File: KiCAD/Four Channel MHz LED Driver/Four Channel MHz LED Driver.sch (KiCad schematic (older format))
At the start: 81 parts, among them J1 Barrel_Jack_Switch, J10 Conn_01x08_Female, J2 Conn_01x02_Female, J3 8P8C_Shielded_x4, J4 Conn_01x05_Female, J5 Conn_01x24_Female, J6 Conn_01x03_Male, J7 Conn_01x24_Female, J8 Conn_01x03_Female, J9 Conn_01x03_Female, M1 Fan_4pin, Q2 SUM70060E, SW1 SW_SPDT, SW2 Pushbutton_with_LED_-_ELUMOAT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, SW3 Pushbutton_with_LED_-_ELUMOAT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, SW4 Pushbutton_with_LED_-_ELUMOAT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, SW5 Pushbutton_with_LED_-_ELUMOAT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, U1 12V boost, U10 LT6200CS8-10, U14 Teensy3.6, U16 SN74LV4T125PWR, U2 ASSR-1218, U3 DPBW06F-05, U4 BDJ0GA5WEFJ-E2, U5 ADP7182AUJZ-1.8-R7, U6 TMUX1204DGSR, U7 ASSR-1218, U8 ASSR-1218, U9 ASSR-1218

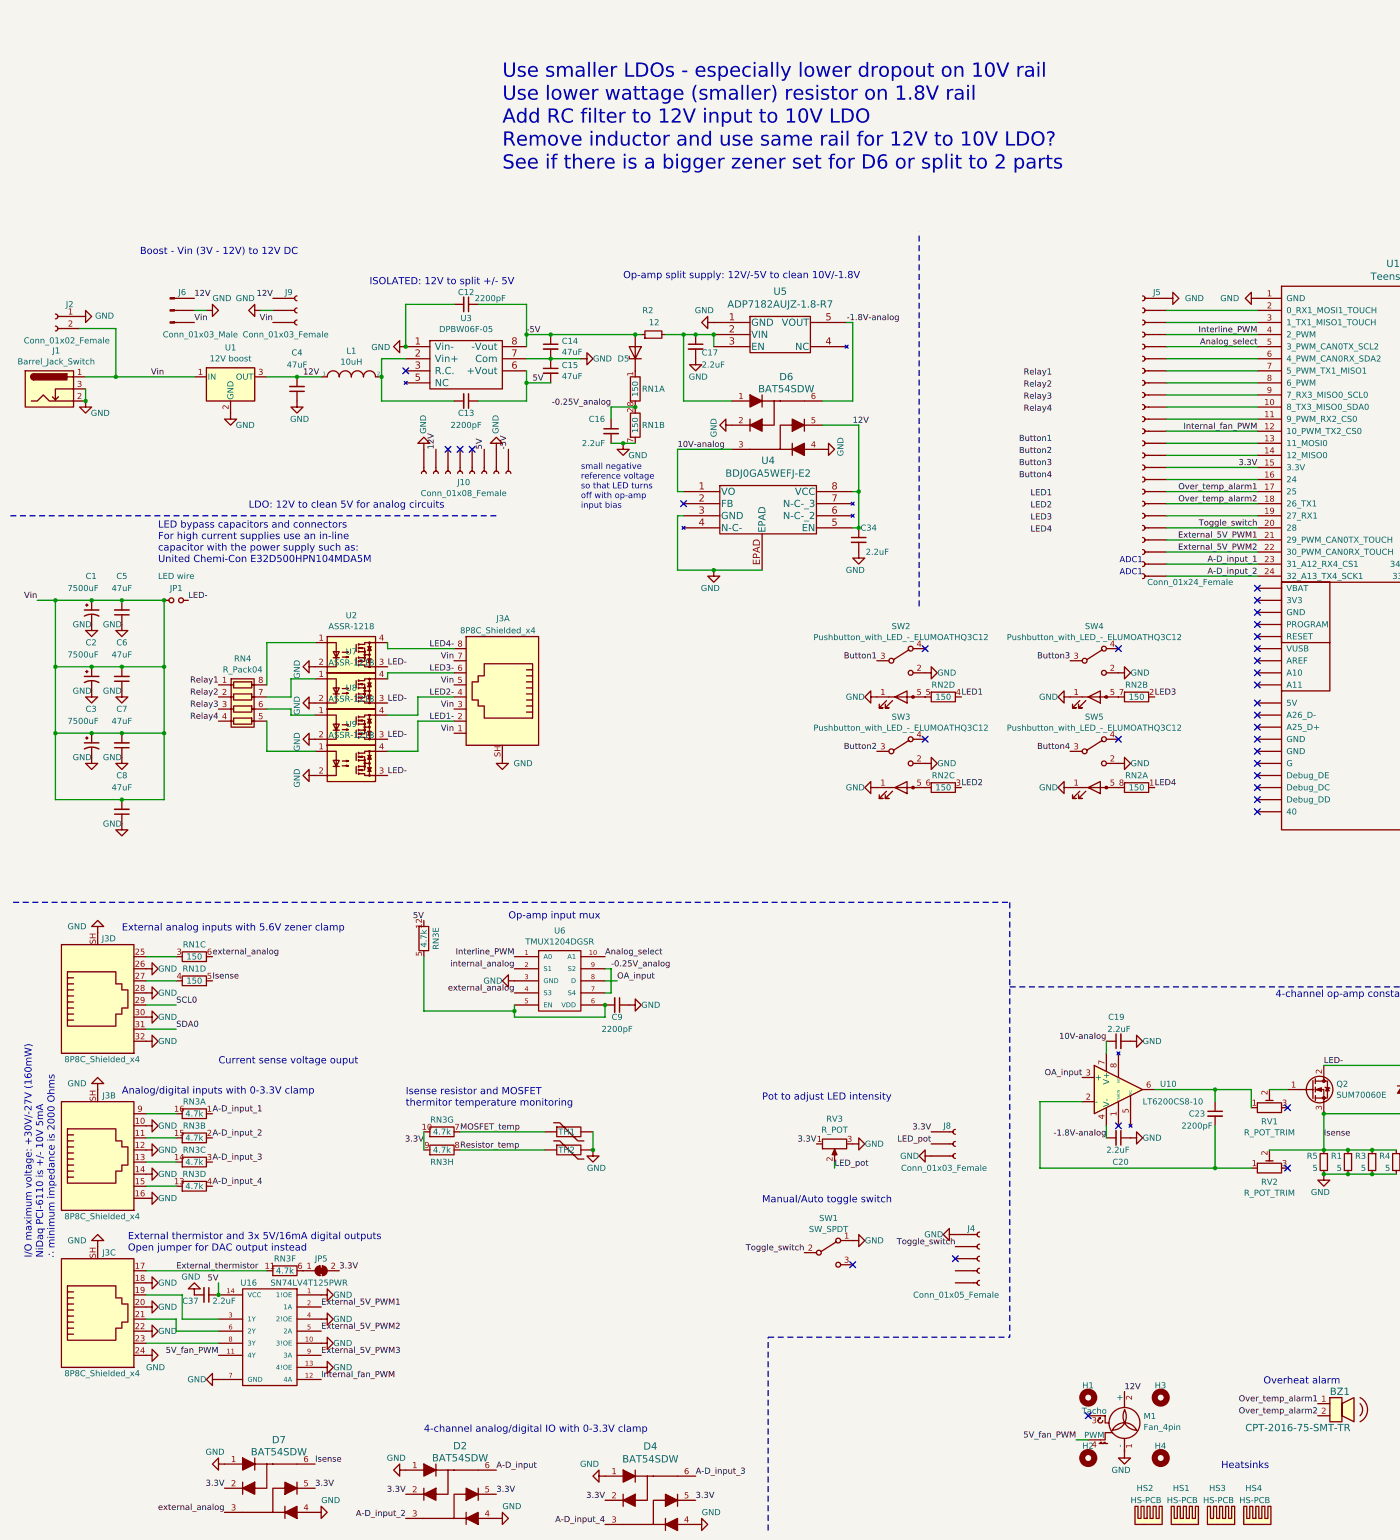
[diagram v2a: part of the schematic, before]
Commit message: Relays connected
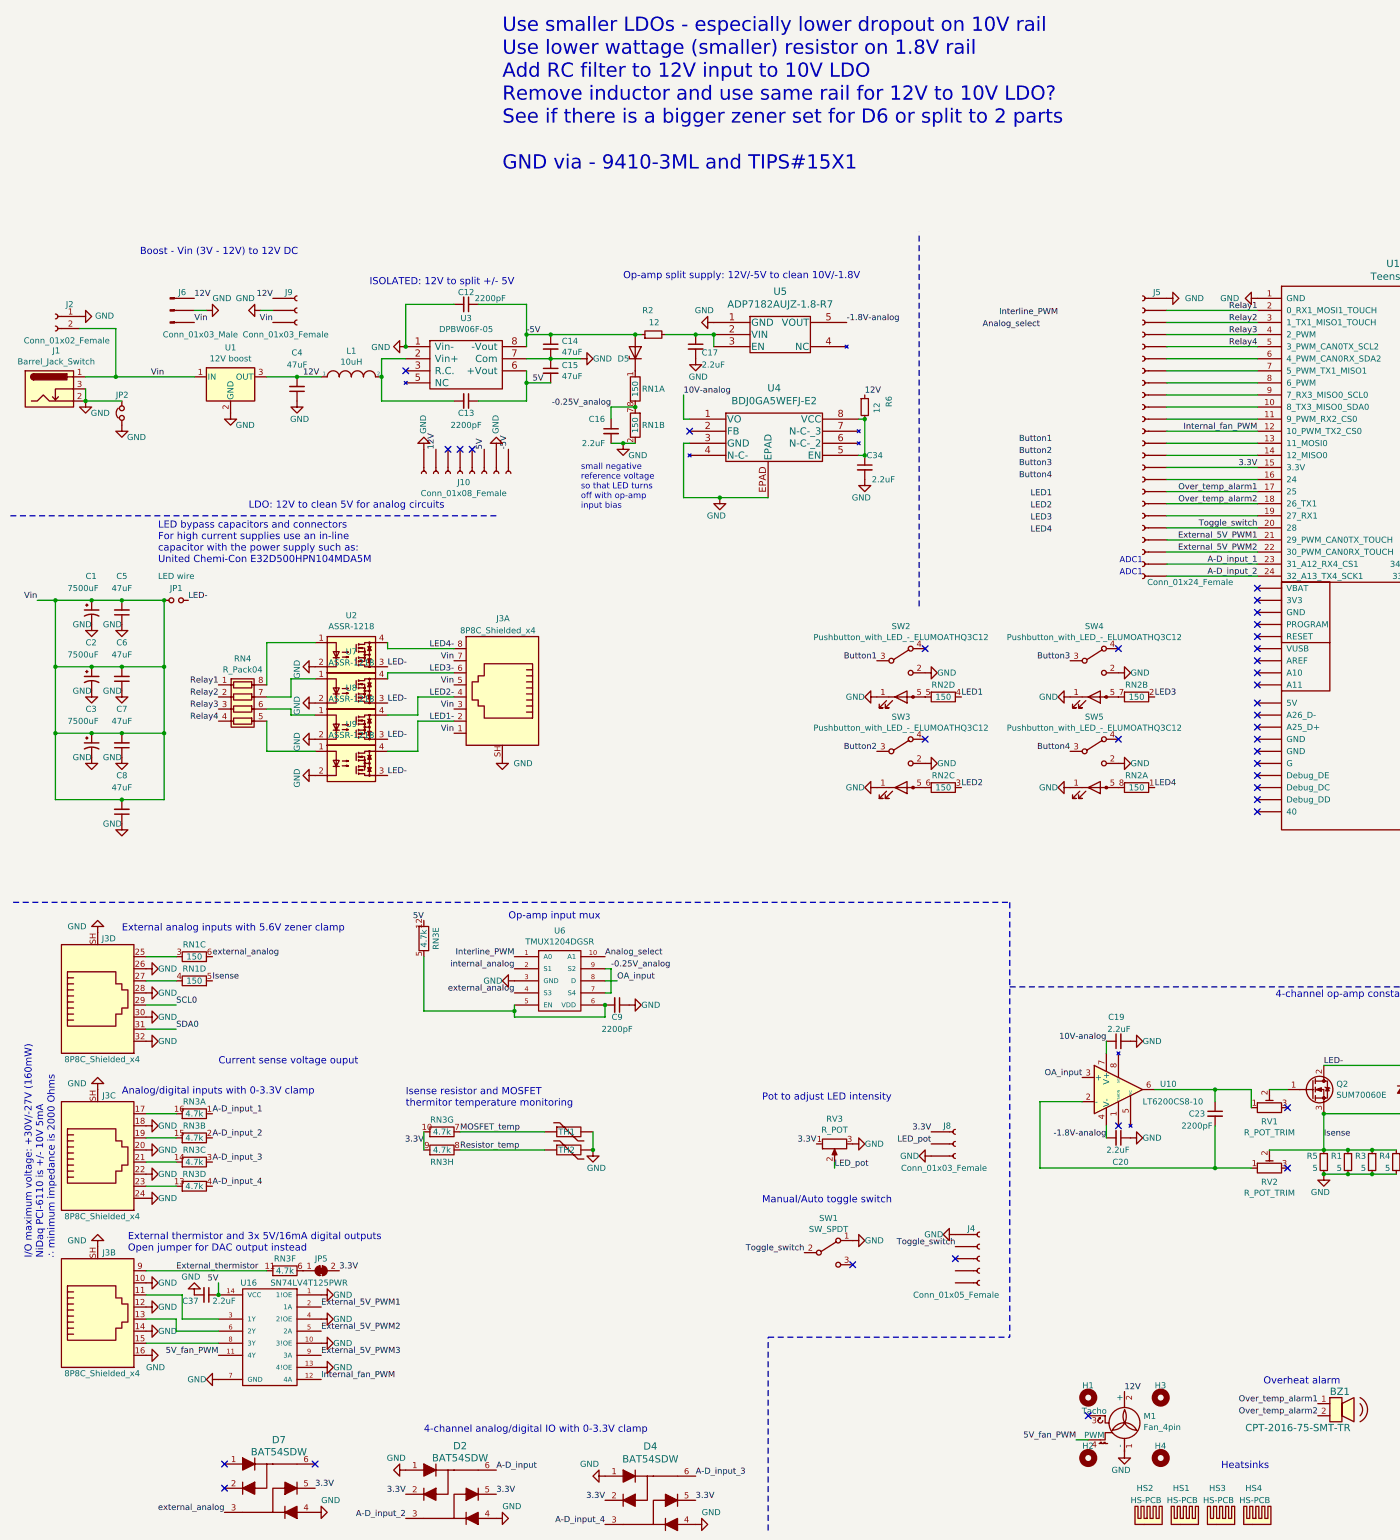
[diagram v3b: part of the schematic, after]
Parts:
- removed D6: BAT54SDW, Package_TO_SOT_SMD:SOT-363_SC-70-6, symbol Custom_parts:BAT54SDW
- added JP2: Jumper_NC_Small, Resistor_SMD:R_1206_3216Metric, symbol Device:Jumper_NC_Small
- added R6: 12, Resistor_SMD:R_1210_3225Metric, symbol Device:R_Small
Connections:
- net -0.25V_analog: now also RN1.7 (R2.2); no longer RN1.2 (R2.1)
- net 12V: now also R6.1; no longer C34.1, U4.5 (EN), U4.8 (VCC)
- net 3.3V: no longer D7.2
- net Analog_select: no longer J5.~, U14.5 (3_PWM_CAN0TX_SCL2)
- net External_thermistor: now also J3.9; no longer J3.17
- net GND: now also RN1.2 (R2.1), JP2.1, JP2.2; no longer D7.1, RN1.7 (R2.2)
- net Interline_PWM: no longer J5.~, U14.4 (2_PWM)
- net Isense: no longer D7.6
- net Relay1: now also J5.~, U14.2 (0_RX1_MOSI1_TOUCH)
- net Relay2: now also J5.~, U14.3 (1_TX1_MISO1_TOUCH)
- net Relay3: now also J5.~, U14.4 (2_PWM)
- net Relay4: now also J5.~, U14.5 (3_PWM_CAN0TX_SCL2)
- net at J3.11: now also U16.3 (1Y); no longer RN3.15 (R2.2)
- net at J3.13: now also U16.6 (2Y); no longer RN3.14 (R3.2)
- net at J3.15: now also U16.8 (3Y); no longer RN3.13 (R4.2)
- net at RN3.16 (R1.2): now also J3.17; no longer J3.9
- net at J3.19: now also RN3.15 (R2.2); no longer U16.3 (1Y)
- net at J3.21: now also RN3.14 (R3.2); no longer U16.6 (2Y)
- net at J3.23: now also RN3.13 (R4.2); no longer U16.8 (3Y)
- new net: C34.1, R6.2, U4.5 (EN), U4.8 (VCC)
- no-connect marks 53 -> 56
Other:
- note added: "Use smaller LDOs - especially lower dropout on 10V rail\nUse lower wattage (smaller) resistor on 1.8V rail\nAdd RC filter to 12V input to 10V LDO\nRemove inductor and use same rail for 12V to 10V LDO?\nSee if there is a bigger zener set for D6 or split to 2 parts\n\nGND via - 9410-3ML and TIPS#15X1"
- note removed: "Use smaller LDOs - especially lower dropout on 10V rail\nUse lower wattage (smaller) resistor on 1.8V rail\nAdd RC filter to 12V input to 10V LDO\nRemove inductor and use same rail for 12V to 10V LDO?\nSee if there is a bigger zener set for D6 or split to 2 parts"
- moved on the sheet: C34, J3B, J3C, U4

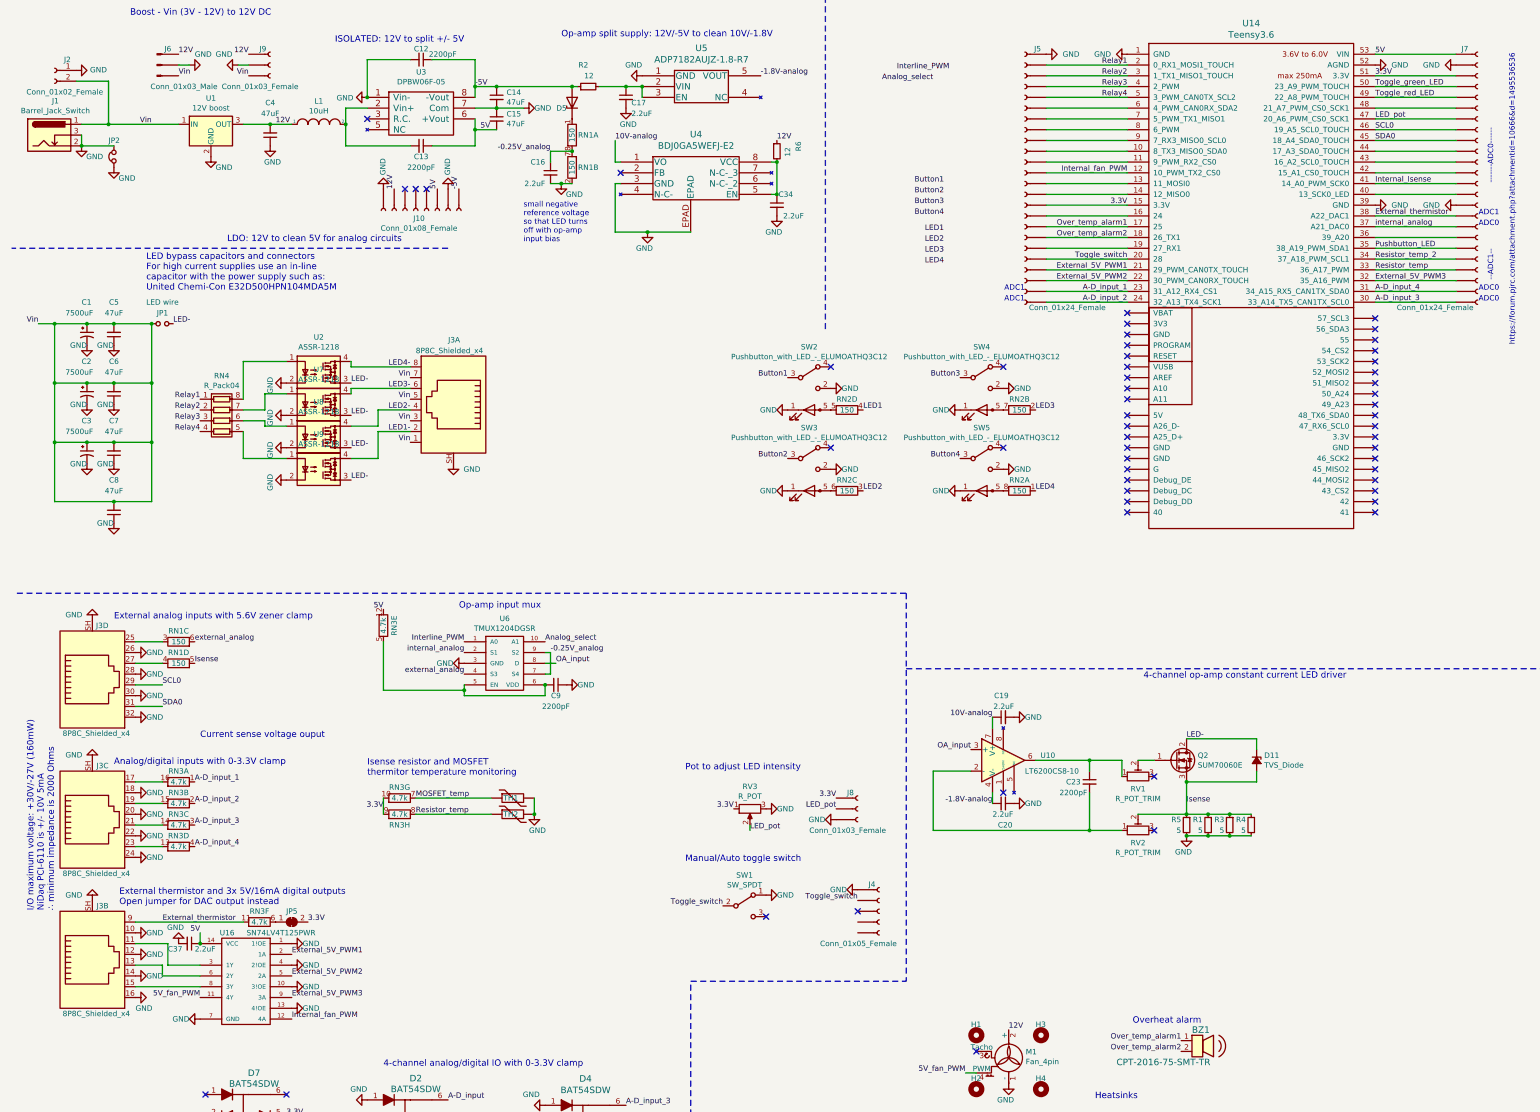
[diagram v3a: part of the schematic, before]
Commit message: 5V PWM level shift output connected
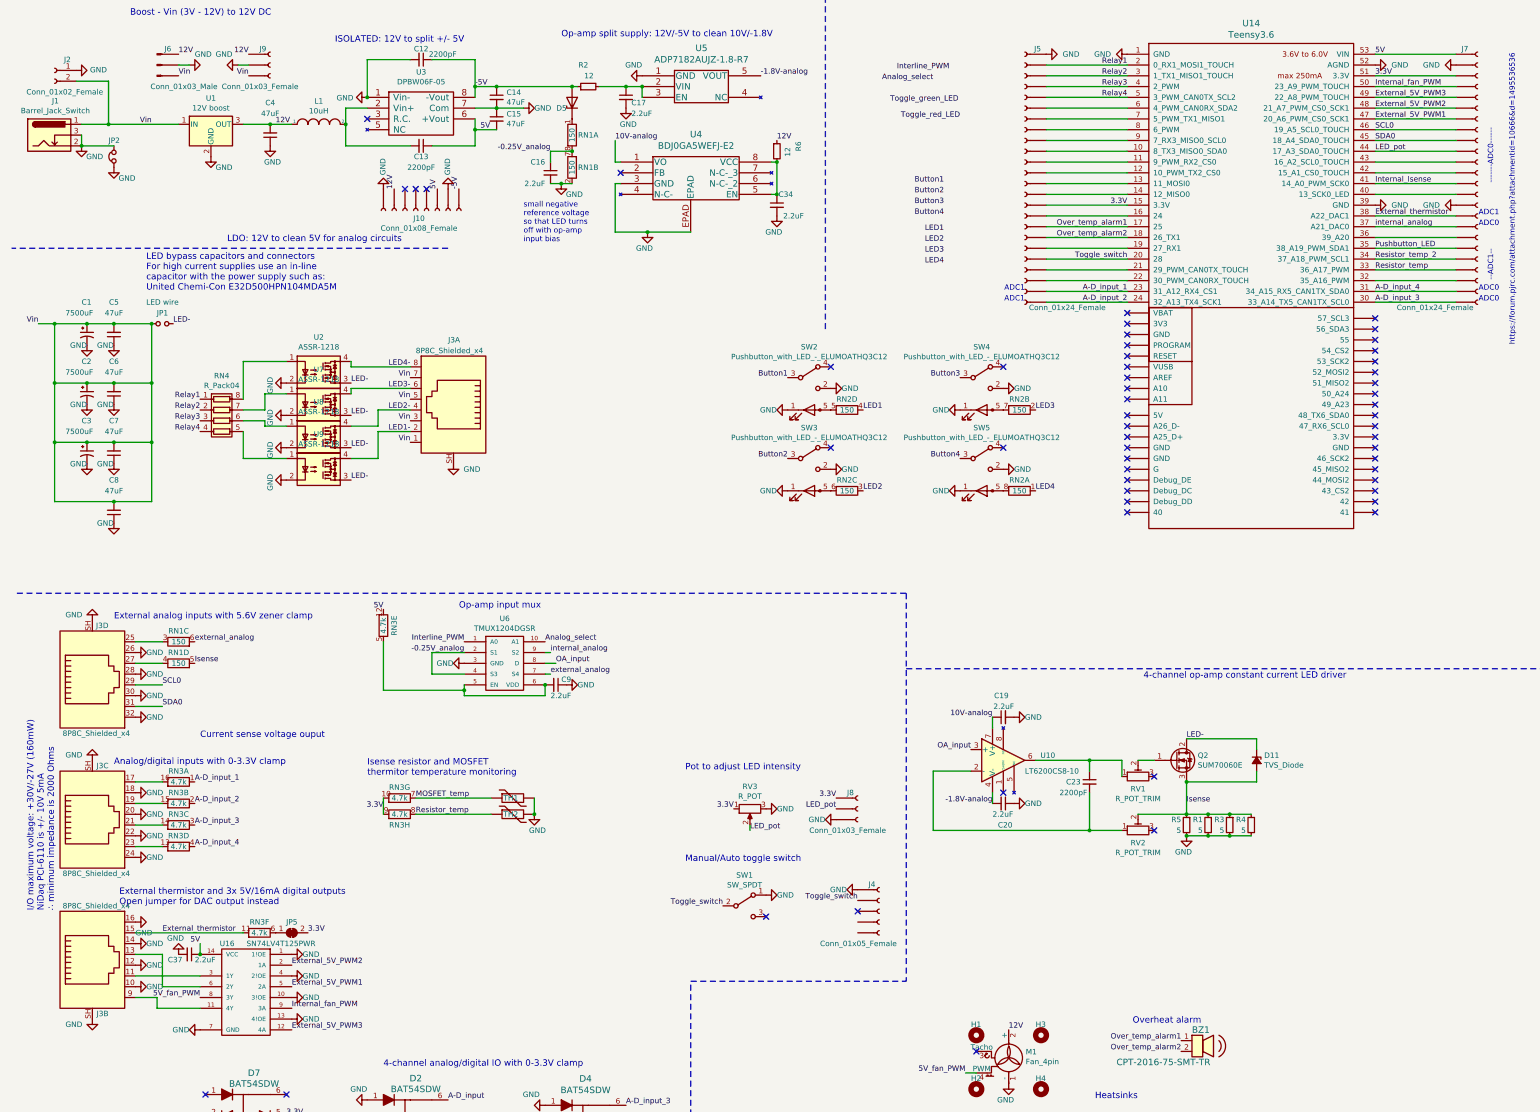
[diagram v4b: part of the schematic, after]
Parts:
- C9: value 2200pF -> 2.2uF; footprint Capacitor_SMD:C_0603_1608Metric -> Custom Footprints:0508_Capacitor; Manufacturer KEMET -> Taiyo Yuden; Part # C0603C222K1RACTU -> TWK212B7225MD-T
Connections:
- net -0.25V_analog: now also U6.2 (S1), U6.4 (S3); no longer U6.7 (S4), U6.9 (S2)
- net 5V_fan_PWM: now also U16.8 (3Y); no longer U16.11 (4Y)
- net External_5V_PWM1: now also J7.~, U14.47 (20_A6_PWM_CS0_SCK1), U16.5 (2A); no longer J5.~, U14.21 (29_PWM_CAN0TX_TOUCH), U16.2 (1A)
- net External_5V_PWM2: now also J7.~, U14.48 (21_A7_PWM_CS0_SCK1), U16.2 (1A); no longer J5.~, U14.22 (30_PWM_CAN0RX_TOUCH), U16.5 (2A)
- net External_5V_PWM3: now also U14.49 (22_A8_PWM_TOUCH), U16.12 (4A); no longer U14.32 (35_A16_PWM), U16.9 (3A)
- net External_thermistor: now also J3.15; no longer J3.9
- net Internal_fan_PWM: now also J7.~, U14.50 (23_A9_PWM_TOUCH), U16.9 (3A); no longer J5.~, U14.12 (10_PWM_TX2_CS0), U16.12 (4A)
- net LED_pot: now also U14.44 (17_A3_SDA0_TOUCH); no longer U14.47 (20_A6_PWM_CS0_SCK1)
- net Toggle_green_LED: no longer J7.~, U14.50 (23_A9_PWM_TOUCH)
- net Toggle_red_LED: no longer J7.~, U14.49 (22_A8_PWM_TOUCH)
- net external_analog: now also U6.7 (S4); no longer U6.4 (S3)
- net internal_analog: now also U6.9 (S2); no longer U6.2 (S1)
- new net: J5.~, U14.12 (10_PWM_TX2_CS0)
- new net: J5.~, U14.21 (29_PWM_CAN0TX_TOUCH)
- new net: J5.~, U14.22 (30_PWM_CAN0RX_TOUCH)
- new net: J7.~, U14.32 (35_A16_PWM)
- new net: J3.9, U16.11 (4Y)
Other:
- moved on the sheet: C37, J3B, JP5, RN3F, U16
